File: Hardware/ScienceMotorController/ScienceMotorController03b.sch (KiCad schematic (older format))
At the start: 17 parts, among them U3 VNH5019A_E

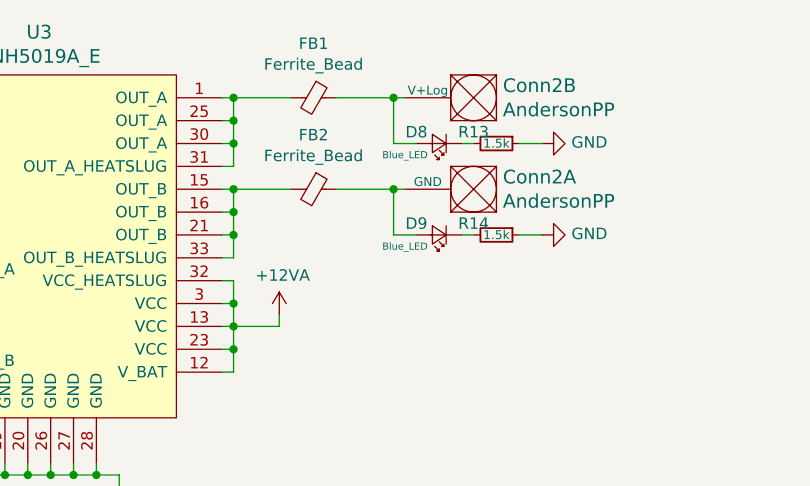
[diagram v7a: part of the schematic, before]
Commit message: assigned most of the footprints
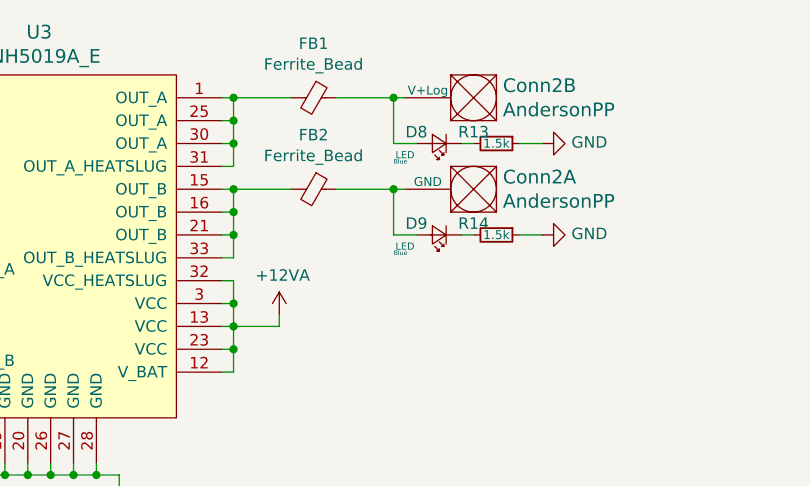
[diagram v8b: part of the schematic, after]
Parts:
- Conn2: footprint (none) -> MRDT_Connectors:Anderson_2_Vertical_Sidy_by_Side
- D7: footprint (none) -> Diode_SMD:D_0603_1608Metric_Pad1.05x0.95mm_HandSolder
- D8, D9: value Blue_LED -> LED; footprint (none) -> LED_SMD:LED_0603_1608Metric_Pad1.05x0.95mm_HandSolder
- R10, R11, R12, R13, R14, R6, R7, R8, R9: footprint (none) -> Resistor_SMD:R_0603_1608Metric_Pad1.05x0.95mm_HandSolder
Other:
- note added: "Blue"
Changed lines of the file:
@@
 F 0 "R10" V 4600 3650 50  0000 C CNN
 F 1 "1k" V 4650 3800 50  0000 C CNN
-F 2 "" H 4650 3800 50  0001 C CNN
+F 2 "Resistor_SMD:R_0603_1608Metric_Pad1.05x0.95mm_HandSolder" H 4650 3800 50  0001 C CNN
 F 3 "~" H 4650 3800 50  0001 C CNN
 	1    4650 3800
@@
 F 0 "R7" V 3850 4050 50  0000 C CNN
 F 1 "1k" V 3950 4050 50  0000 C CNN
-F 2 "" H 3950 4050 50  0001 C CNN
+F 2 "Resistor_SMD:R_0603_1608Metric_Pad1.05x0.95mm_HandSolder" H 3950 4050 50  0001 C CNN
 F 3 "~" H 3950 4050 50  0001 C CNN
 	1    3950 4050
@@
 F 0 "D7" V 3150 3900 50  0000 R CNN
 F 1 "D_Zener_Small" V 3050 3950 50  0000 R CNN
-F 2 "" V 3100 4050 50  0001 C CNN
+F 2 "Diode_SMD:D_0603_1608Metric_Pad1.05x0.95mm_HandSolder" V 3100 4050 50  0001 C CNN
 F 3 "~" V 3100 4050 50  0001 C CNN
 	1    3100 4050
@@
 F 0 "R6" V 3550 3900 50  0000 C CNN
 F 1 "10k" V 3650 3900 50  0000 C CNN
-F 2 "" H 3650 3900 50  0001 C CNN
+F 2 "Resistor_SMD:R_0603_1608Metric_Pad1.05x0.95mm_HandSolder" H 3650 3900 50  0001 C CNN
 F 3 "~" H 3650 3900 50  0001 C CNN
 	1    3650 3900
@@
 F 0 "R11" V 4600 3850 50  0000 C CNN
 F 1 "1k" V 4650 4000 50  0000 C CNN
-F 2 "" H 4650 4000 50  0001 C CNN
+F 2 "Resistor_SMD:R_0603_1608Metric_Pad1.05x0.95mm_HandSolder" H 4650 4000 50  0001 C CNN
 F 3 "~" H 4650 4000 50  0001 C CNN
 	1    4650 4000
@@
 F 0 "R9" V 4600 3450 50  0000 C CNN
 F 1 "1k" V 4650 3600 50  0000 C CNN
-F 2 "" H 4650 3600 50  0001 C CNN
+F 2 "Resistor_SMD:R_0603_1608Metric_Pad1.05x0.95mm_HandSolder" H 4650 3600 50  0001 C CNN
 F 3 "~" H 4650 3600 50  0001 C CNN
 	1    4650 3600
@@
 F 0 "R8" V 4600 3350 50  0000 C CNN
 F 1 "1k" V 4650 3500 50  0000 C CNN
-F 2 "" H 4650 3500 50  0001 C CNN
+F 2 "Resistor_SMD:R_0603_1608Metric_Pad1.05x0.95mm_HandSolder" H 4650 3500 50  0001 C CNN
 F 3 "~" H 4650 3500 50  0001 C CNN
 	1    4650 3500
@@
 F 0 "R12" V 4600 3950 50  0000 C CNN
 F 1 "1k" V 4650 4100 50  0000 C CNN
-F 2 "" H 4650 4100 50  0001 C CNN
+F 2 "Resistor_SMD:R_0603_1608Metric_Pad1.05x0.95mm_HandSolder" H 4650 4100 50  0001 C CNN
 F 3 "~" H 4650 4100 50  0001 C CNN
 	1    4650 4100
@@
 F 0 "Conn2" H 7672 3197 60  0000 R CNN
 F 1 "AndersonPP" H 7672 3303 60  0000 R CNN
-F 2 "" H 7550 2600 60  0001 C CNN
+F 2 "MRDT_Connectors:Anderson_2_Vertical_Sidy_by_Side" H 7550 2600 60  0001 C CNN
 F 3 "" H 7550 2600 60  0001 C CNN
 	1    7700 3150
@@
 F 0 "Conn2" H 7672 2797 60  0000 R CNN
 F 1 "AndersonPP" H 7672 2903 60  0000 R CNN
-F 2 "" H 7550 2200 60  0001 C CNN
+F 2 "MRDT_Connectors:Anderson_2_Vertical_Sidy_by_Side" H 7550 2200 60  0001 C CNN
 F 3 "" H 7550 2200 60  0001 C CNN
 	2    7700 2750
@@
 AR Path="/5F7148FA/5FA34AD5/5FA5B816" Ref="D8"  Part="1"
 F 0 "D8" H 7550 3000 50  0000 C CNN
-F 1 "Blue_LED" H 7600 3100 31  0000 C CNN
-F 2 "" V 7450 3050 50  0001 C CNN
+F 1 "LED" H 7600 3100 31  0000 C CNN
+F 2 "LED_SMD:LED_0603_1608Metric_Pad1.05x0.95mm_HandSolder" V 7450 3050 50  0001 C CNN
 F 3 "~" V 7450 3050 50  0001 C CNN
 	1    7450 3050
@@
 AR Path="/5F7148FA/5FA34AD5/5FA5B81C" Ref="D9"  Part="1"
 F 0 "D9" H 7550 3400 50  0000 C CNN
-F 1 "Blue_LED" H 7600 3500 31  0000 C CNN
-F 2 "" V 7450 3450 50  0001 C CNN
+F 1 "LED" H 7600 3500 31  0000 C CNN
+F 2 "LED_SMD:LED_0603_1608Metric_Pad1.05x0.95mm_HandSolder" V 7450 3450 50  0001 C CNN
 F 3 "~" V 7450 3450 50  0001 C CNN
 	1    7450 3450
@@
 F 0 "R14" V 7650 3350 50  0000 C CNN
 F 1 "1.5k" V 7700 3450 39  0000 C CNN
-F 2 "" H 7700 3450 50  0001 C CNN
+F 2 "Resistor_SMD:R_0603_1608Metric_Pad1.05x0.95mm_HandSolder" H 7700 3450 50  0001 C CNN
 F 3 "~" H 7700 3450 50  0001 C CNN
 	1    7700 3450
@@
 F 0 "R13" V 7650 2950 50  0000 C CNN
 F 1 "1.5k" V 7700 3050 39  0000 C CNN
-F 2 "" H 7700 3050 50  0001 C CNN
+F 2 "Resistor_SMD:R_0603_1608Metric_Pad1.05x0.95mm_HandSolder" H 7700 3050 50  0001 C CNN
 F 3 "~" H 7700 3050 50  0001 C CNN
 	1    7700 3050
@@
 Text HLabel 4400 4000 0    50   Output ~ 0
 3.3V
+Text Notes 7250 3150 0    20   ~ 0
+Blue
+Text Notes 7250 3550 0    20   ~ 0
+Blue
 $EndSCHEMATC
